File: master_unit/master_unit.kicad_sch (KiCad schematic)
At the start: 2 parts, among them U1 DEV-15583

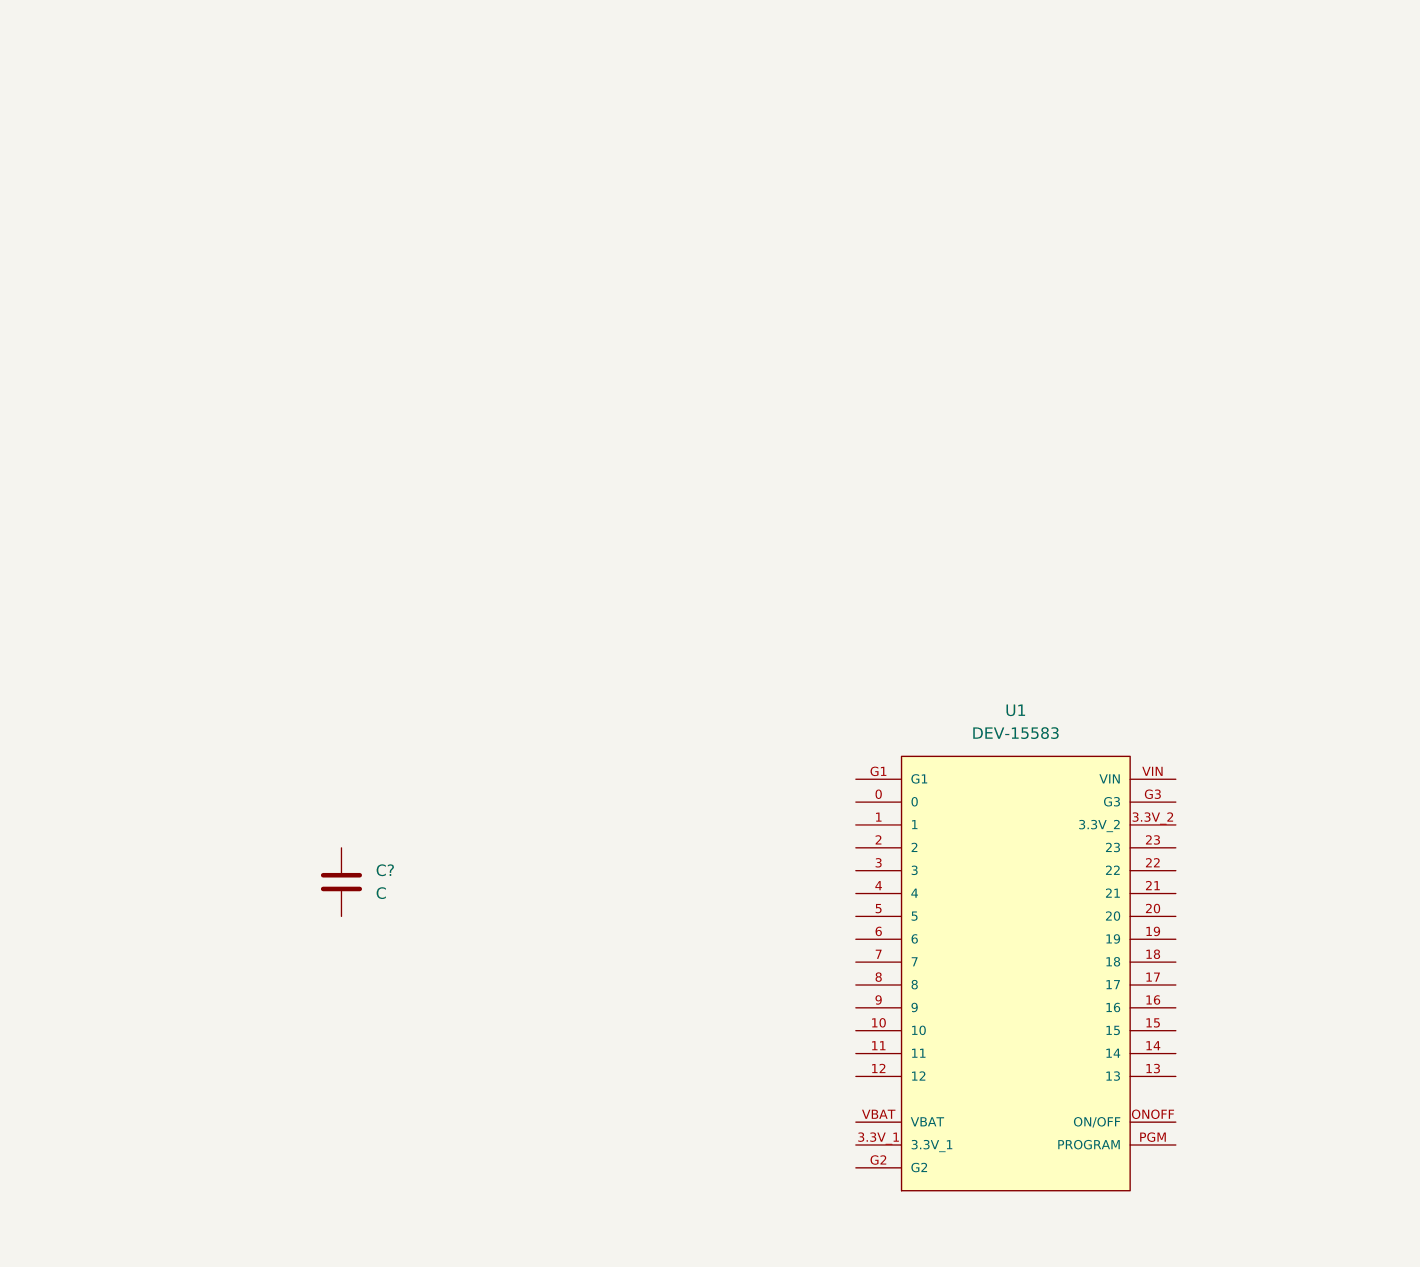
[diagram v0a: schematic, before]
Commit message: included thvd8000 and connectors for power supply
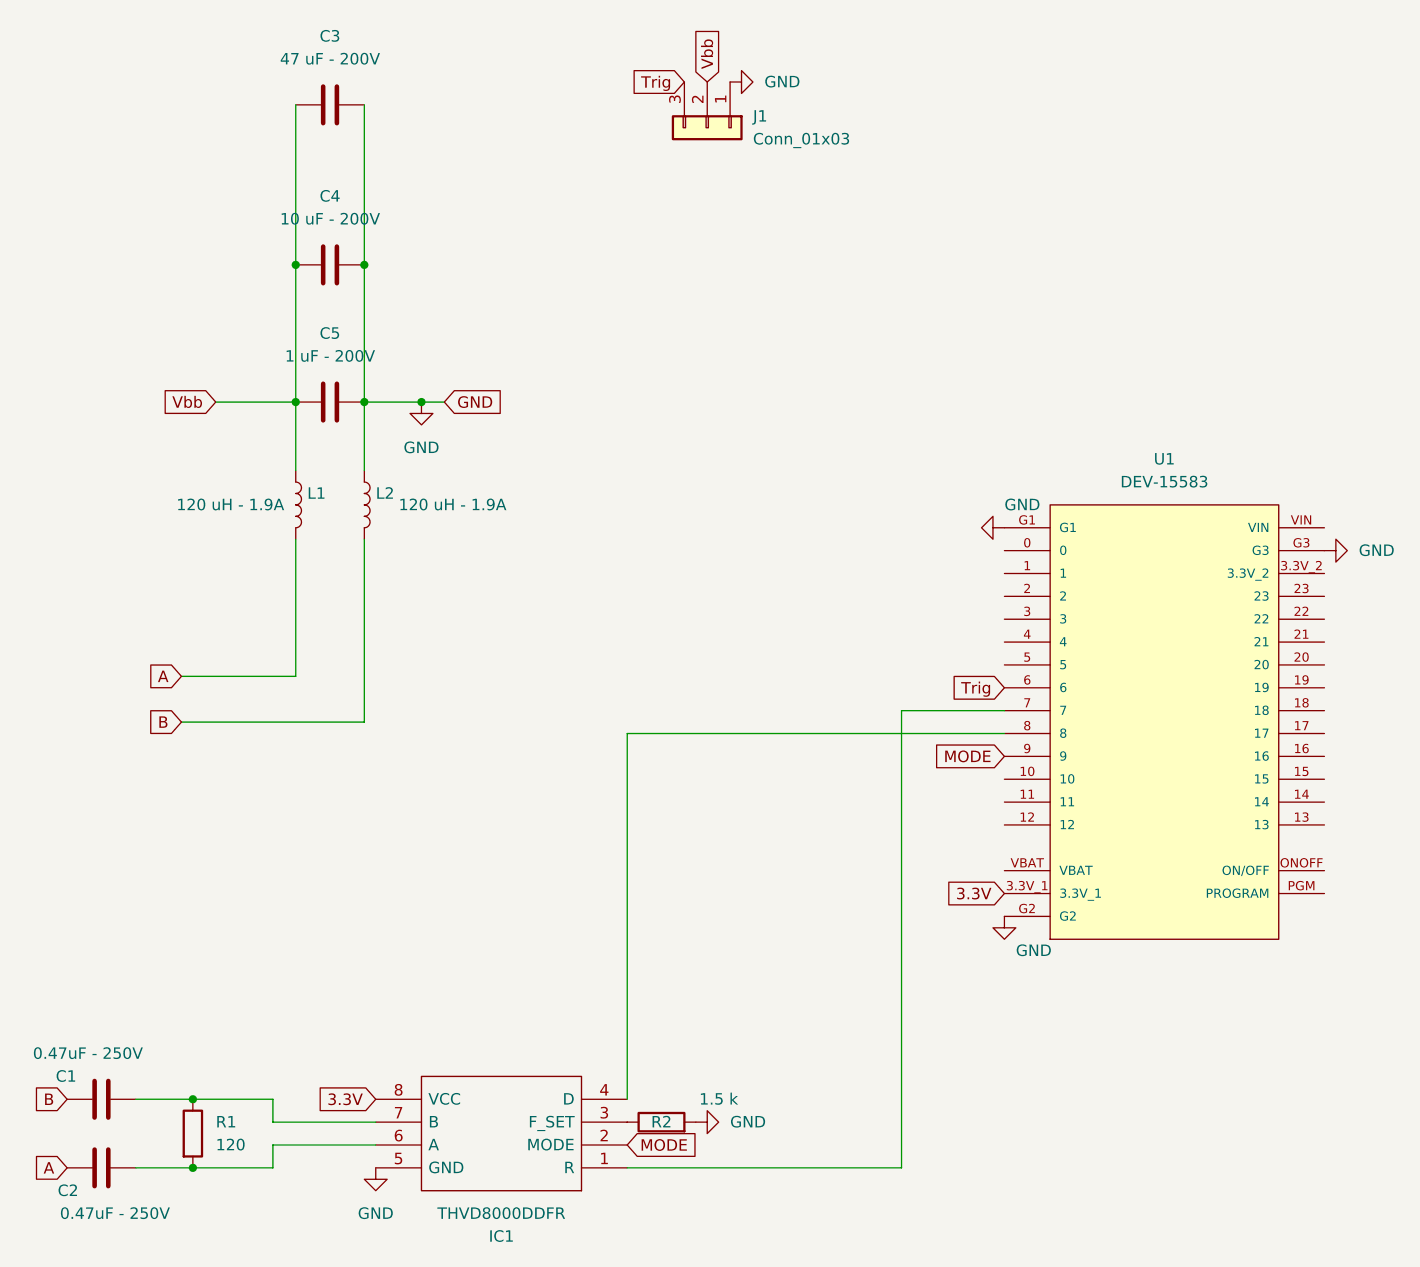
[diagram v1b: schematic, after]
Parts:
- added C2: 0.47uF - 250V, Capacitor_SMD:C_1210_3225Metric, symbol Device:C
- added C3: 47 uF - 200V, Capacitor_THT:CP_Radial_D10.0mm_P5.00mm, symbol Device:C
- added C4: 10 uF - 200V, Capacitor_THT:CP_Radial_D8.0mm_P3.50mm, symbol Device:C
- added C5: 1 uF - 200V, Capacitor_SMD:C_1812_4532Metric, symbol Device:C
- added IC1: THVD8000DDFR, SOT65P280X110-8N, symbol THVD8000:THVD8000DDFR
- added J1: Conn_01x03, Connector:Banana_Jack_3Pin, symbol Connector_Generic:Conn_01x03
- added L1, L2: 120 uH - 1.9A, MSS1278-124KLD:INDPM120120X805N, symbol Device:L
- added R1: 120, Resistor_SMD:R_0603_1608Metric, symbol Device:R
- added R2: 1.5 k, Resistor_SMD:R_0603_1608Metric, symbol Device:R
- C1: renamed from C?; value C -> 0.47uF - 250V; footprint (none) -> Capacitor_SMD:C_1210_3225Metric
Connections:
- net 3.3V: now reaches U1.3.3V_1
- net 3.3V: now also IC1.8 (VCC)
- net Trig: now reaches U1.6
- net Trig: now also J1.3 (Pin_3)
- net at U1.7: now also IC1.1 (R)
- net at U1.8: now also IC1.4 (D)
- net MODE: now reaches U1.9
- net MODE: now also IC1.2 (MODE)
- net GND: now reaches U1.G1
- net GND: now also U1.G2, U1.G3, C3.2, C4.2, C5.2, IC1.5 (GND), J1.1 (Pin_1), L2.1, R2.2
- net at C1.1: now also IC1.7 (B), R1.1
- net B: now reaches C1.2
- net B: now also L2.2
- new net: C2.2, IC1.6 (A), R1.2
- new net: IC1.3 (F_SET), R2.1
- new net A: C2.1, L1.2
- new net Vbb: C3.1, C4.1, C5.1, J1.2 (Pin_2), L1.1
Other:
- moved on the sheet: C1, U1

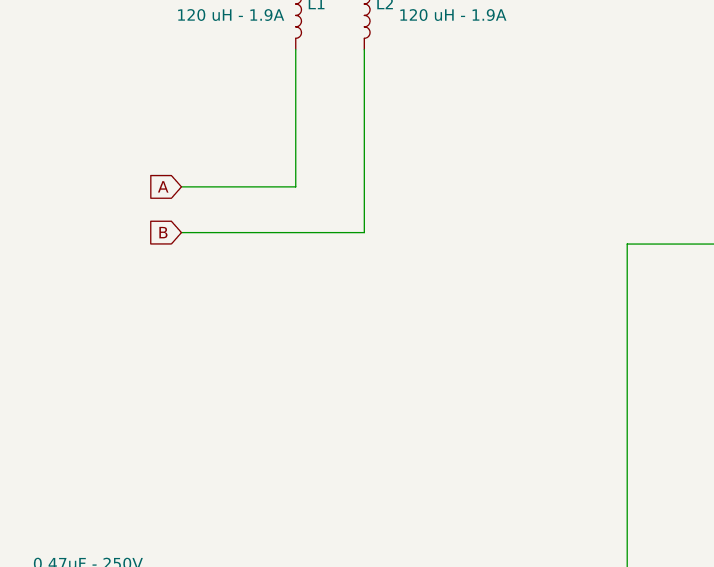
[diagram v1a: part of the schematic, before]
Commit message: preliminary layout
All basic component are there and a basic layout is performed.
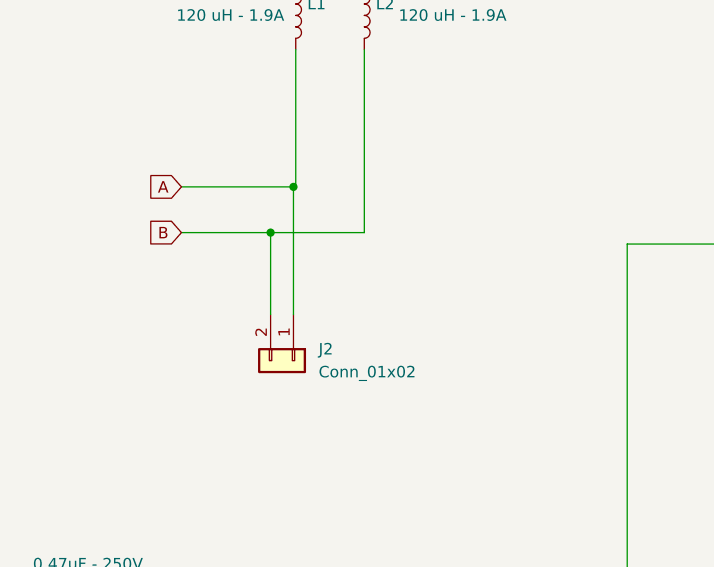
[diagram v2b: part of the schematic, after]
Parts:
- added J2: Conn_01x02, Connector:Banana_Jack_2Pin, symbol Connector_Generic:Conn_01x02
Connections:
- net A: now also J2.1 (Pin_1)
- net B: now also J2.2 (Pin_2)
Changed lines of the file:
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@@
   (junction (at 129.54 137.16) (diameter 0) (color 0 0 0 0)
   )
+  (junction (at 140.716 90.17) (diameter 0) (color 0 0 0 0)
+  )
   (junction (at 140.97 44.45) (diameter 0) (color 0 0 0 0)
   )
   (junction (at 129.54 144.78) (diameter 0) (color 0 0 0 0)
   )
+  (junction (at 138.176 95.25) (diameter 0) (color 0 0 0 0)
+  )
   (junction (at 140.97 59.69) (diameter 0) (color 0 0 0 0)
   )
@@
     (stroke (width 0) (type default) (color 0 0 0 0))
   )
+  (wire (pts (xy 140.716 90.17) (xy 140.97 90.17))
+    (stroke (width 0) (type default) (color 0 0 0 0))
+  )
   (wire (pts (xy 154.94 59.69) (xy 157.48 59.69))
     (stroke (width 0) (type default) (color 0 0 0 0))
   )
-  (wire (pts (xy 128.27 90.17) (xy 140.97 90.17))
+  (wire (pts (xy 128.27 90.17) (xy 140.716 90.17))
     (stroke (width 0) (type default) (color 0 0 0 0))
   )
@@
     (stroke (width 0) (type default) (color 0 0 0 0))
   )
-  (wire (pts (xy 128.27 95.25) (xy 148.59 95.25))
+  (wire (pts (xy 128.27 95.25) (xy 138.176 95.25))
     (stroke (width 0) (type default) (color 0 0 0 0))
   )
@@
     (stroke (width 0) (type default) (color 0 0 0 0))
   )
+  (wire (pts (xy 132.08 59.69) (xy 140.97 59.69))
+    (stroke (width 0) (type default) (color 0 0 0 0))
+  )
+  (wire (pts (xy 140.716 90.17) (xy 140.716 104.394))
+    (stroke (width 0) (type default) (color 0 0 0 0))
+  )
   (wire (pts (xy 177.8 137.16) (xy 177.8 96.52))
     (stroke (width 0) (type default) (color 0 0 0 0))
@@
     (stroke (width 0) (type default) (color 0 0 0 0))
   )
+  (wire (pts (xy 138.176 95.25) (xy 148.59 95.25))
+    (stroke (width 0) (type default) (color 0 0 0 0))
+  )
+  (wire (pts (xy 138.176 104.394) (xy 138.176 95.25))
+    (stroke (width 0) (type default) (color 0 0 0 0))
+  )
   (wire (pts (xy 149.86 139.7) (xy 138.43 139.7))
-    (stroke (width 0) (type default) (color 0 0 0 0))
-  )
-  (wire (pts (xy 132.08 59.69) (xy 140.97 59.69))
     (stroke (width 0) (type default) (color 0 0 0 0))
   )
@@
     (pin "1")
   )
+  (symbol (lib_id "Connector_Generic:Conn_01x02") (at 140.716 109.474 270) (unit 1)
+    (in_bom yes) (on_board yes) (fields_autoplaced)
+    (property "Reference" "J2" (id 0) (at 143.51 108.2039 90)
+      (effects (font (size 1.27 1.27)) (justify left))
+    )
+    (property "Value" "Conn_01x02" (id 1) (at 143.51 110.7439 90)
+      (effects (font (size 1.27 1.27)) (justify left))
+    )
+    (property "Footprint" "Connector:Banana_Jack_2Pin" (id 2) (at 140.716 109.474 0)
+      (effects (font (size 1.27 1.27)) hide)
+    )
+    (property "Datasheet" "~" (id 3) (at 140.716 109.474 0)
+      (effects (font (size 1.27 1.27)) hide)
+    )
+    (pin "1")
+    (pin "2")
+  )
   (symbol (lib_id "power:GND") (at 185.42 139.7 90) (unit 1)
     (in_bom yes) (on_board yes) (fields_autoplaced)
@@
       (reference "J1") (unit 1) (value "Conn_01x03") (footprint "Connector:Banana_Jack_3Pin")
     )
+    (path "/e73067c5-0bf4-4f44-be33-c28f7b06adae"
+      (reference "J2") (unit 1) (value "Conn_01x02") (footprint "Connector:Banana_Jack_2Pin")
+    )
     (path "/865ad547-0179-4f42-abaf-2d73aa3ceb14"
